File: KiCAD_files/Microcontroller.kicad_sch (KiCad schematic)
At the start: 79 parts, among them J403 RJ45_LED_Shielded, J404 RJ45_LED_Shielded, J801 Conn_01x04, U401 OwnTech_SPIN, U402 TCAN334GDR, U405 LTC2850xS8, U406 OPA2277, U410 TS5A3357DCUT

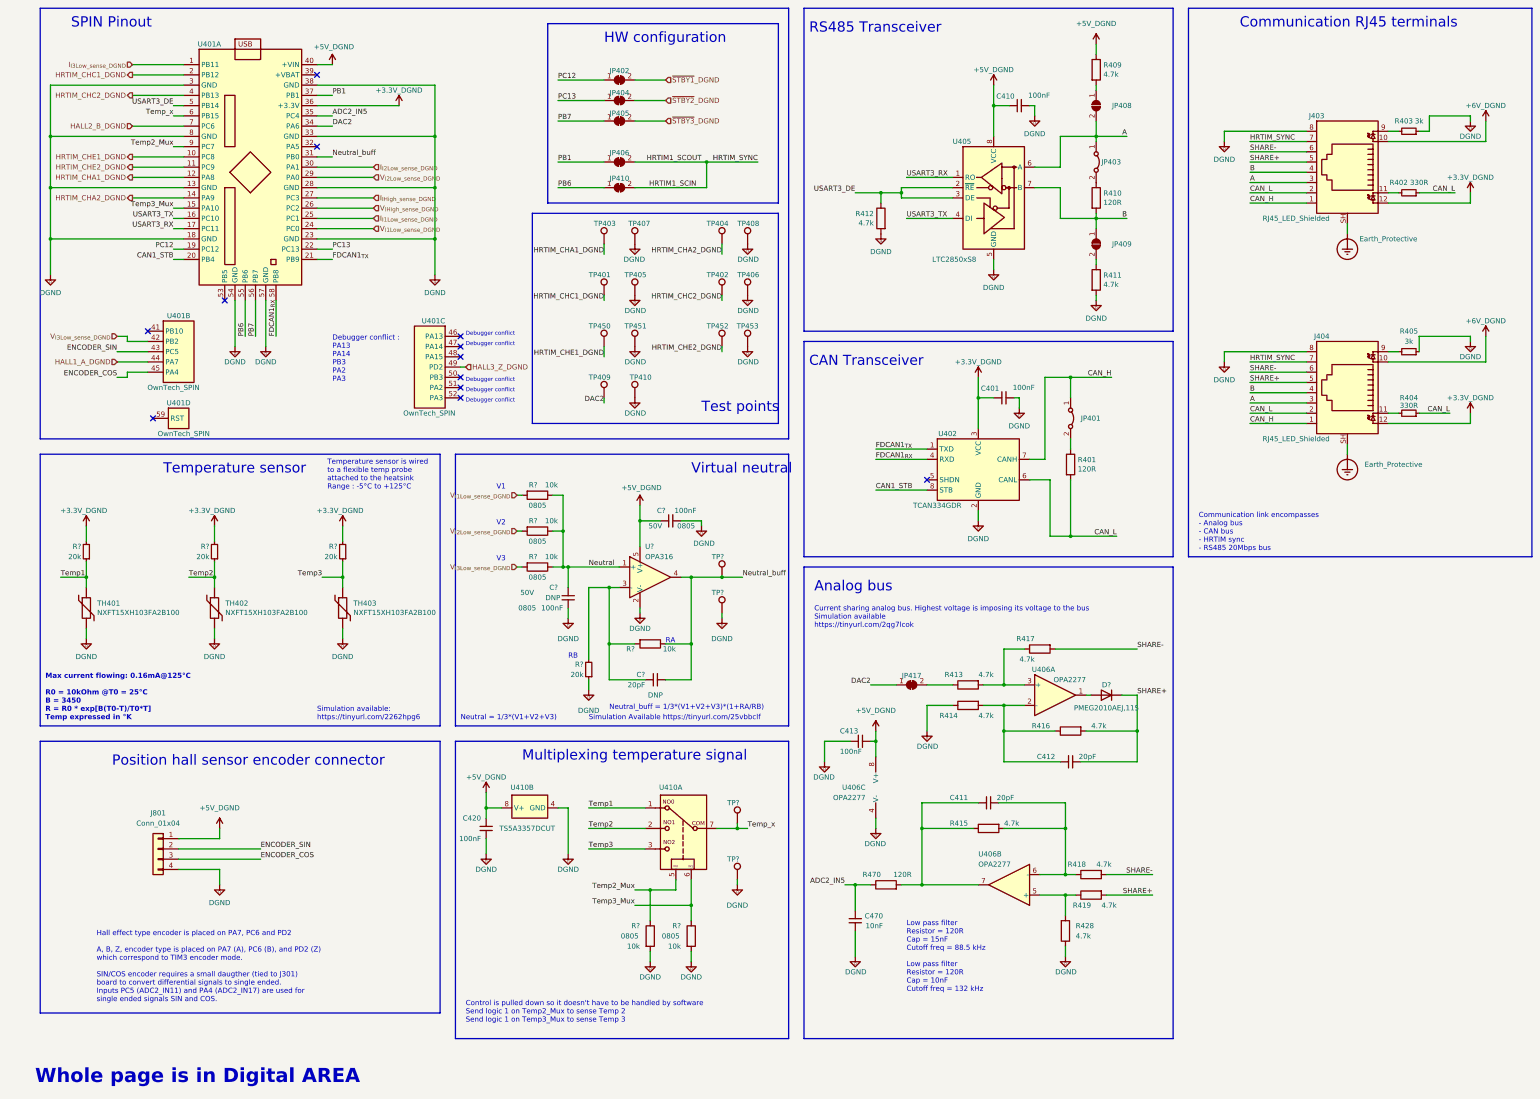
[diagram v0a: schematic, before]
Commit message: Added netclasses and ERC rules for isolation clearances
Signed-off-by: Jean Alinei <jean.alinei@laas.fr>
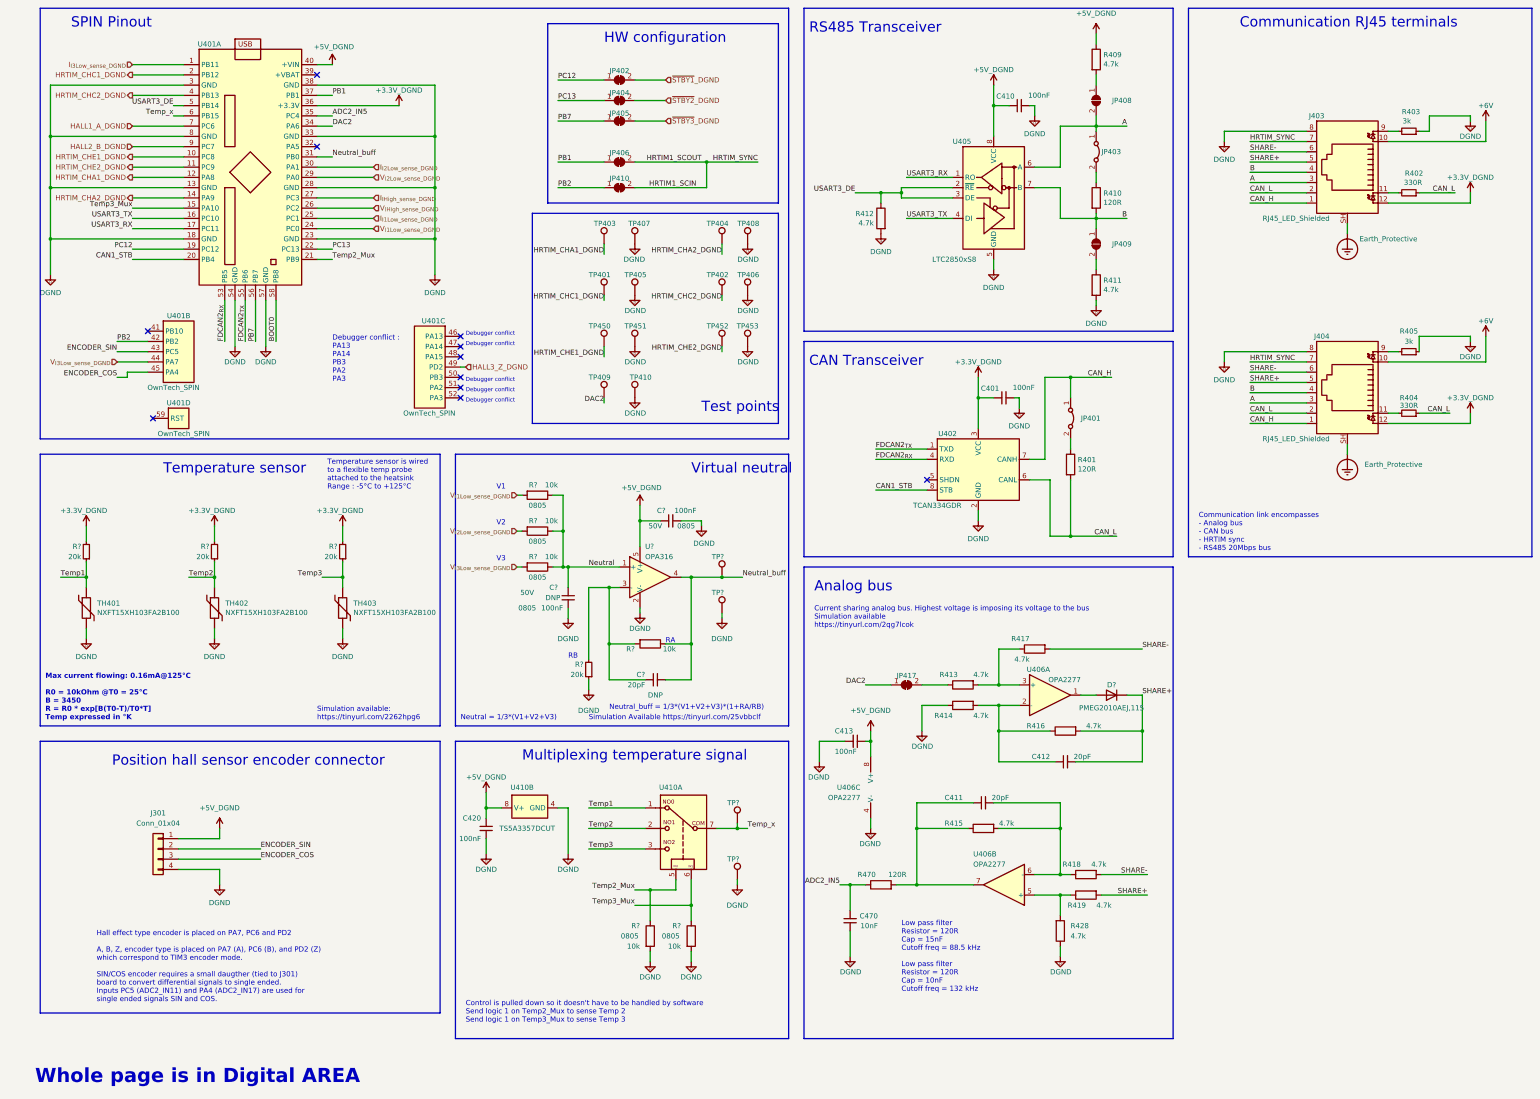
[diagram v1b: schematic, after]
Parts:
- renumbered J801 to J301
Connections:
- net HALL1_A_DGND: now also U401.7 (PC6); no longer U401.44 (PA7)
- net HALL2_B_DGND: now also U401.9 (PC7); no longer U401.7 (PC6)
- net Temp2_Mux: now also U401.21 (PB9); no longer U401.9 (PC7)
- net V_{I3Low_sense_DGND}: now also U401.44 (PA7); no longer U401.42 (PB2)
- net FDCAN2_{RX}: now reaches U401.53 (PB5)
- net FDCAN2_{RX}: now also U402.4 (RXD)
- net FDCAN1_{RX} renamed BOOT0
- net BOOT0: no longer U402.4 (RXD)
- net FDCAN1_{TX} renamed FDCAN2_{TX}
- net FDCAN2_{TX}: now also U401.55 (PB6); no longer U401.21 (PB9)
- net PB6 renamed PB2
- net PB2: now also U401.42 (PB2); no longer U401.55 (PB6)
- no-connect marks 12 -> 11
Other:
- moved on the sheet: C411, C412, C413, C470, D?, JP403, JP408, JP417, R409, R411, R413, R414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
